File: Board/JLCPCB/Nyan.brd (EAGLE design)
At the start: 86 x 26 mm, 64 parts, among them Q1 8M, Q2 32768, U1 R-78C5.0-1.0, U3 A4988_STEP, U4 MAX6966, U5 ST3485, U6 74HCT541PW, U7 74HCT541PW, U8 STM32F10XCXT6, X1 WR-WTB2.0-2_THT-VER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

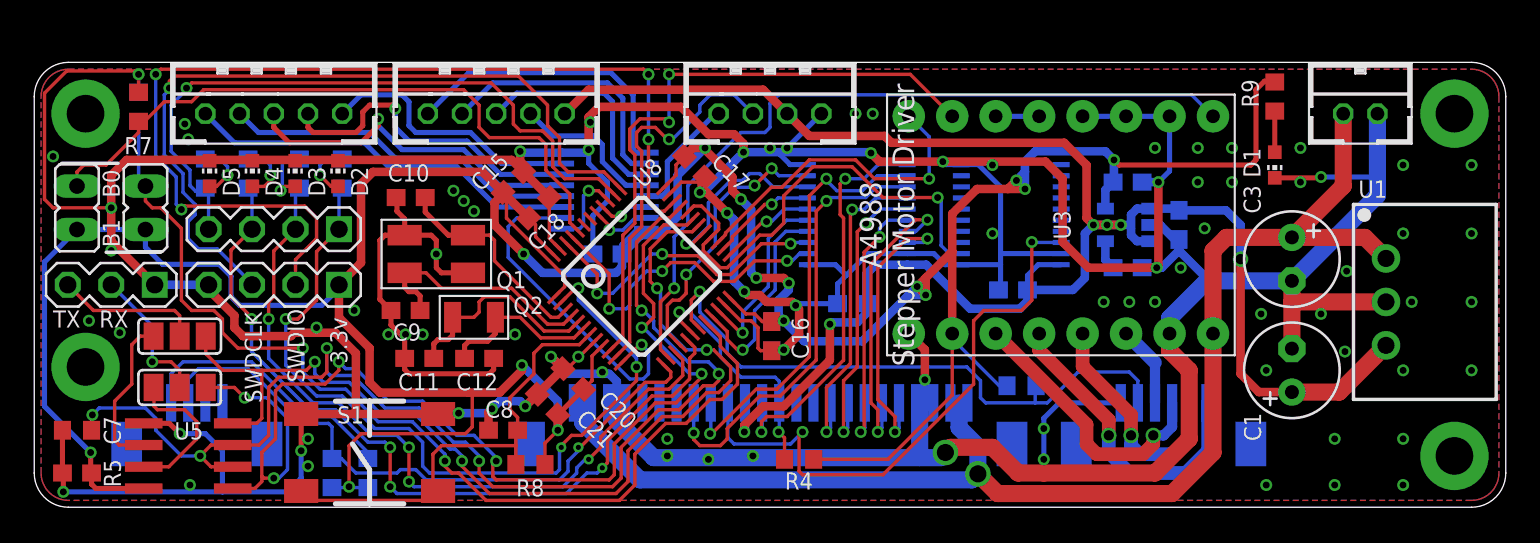
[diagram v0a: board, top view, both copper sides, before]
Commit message: [Board] Silkscreen done, DRC checked
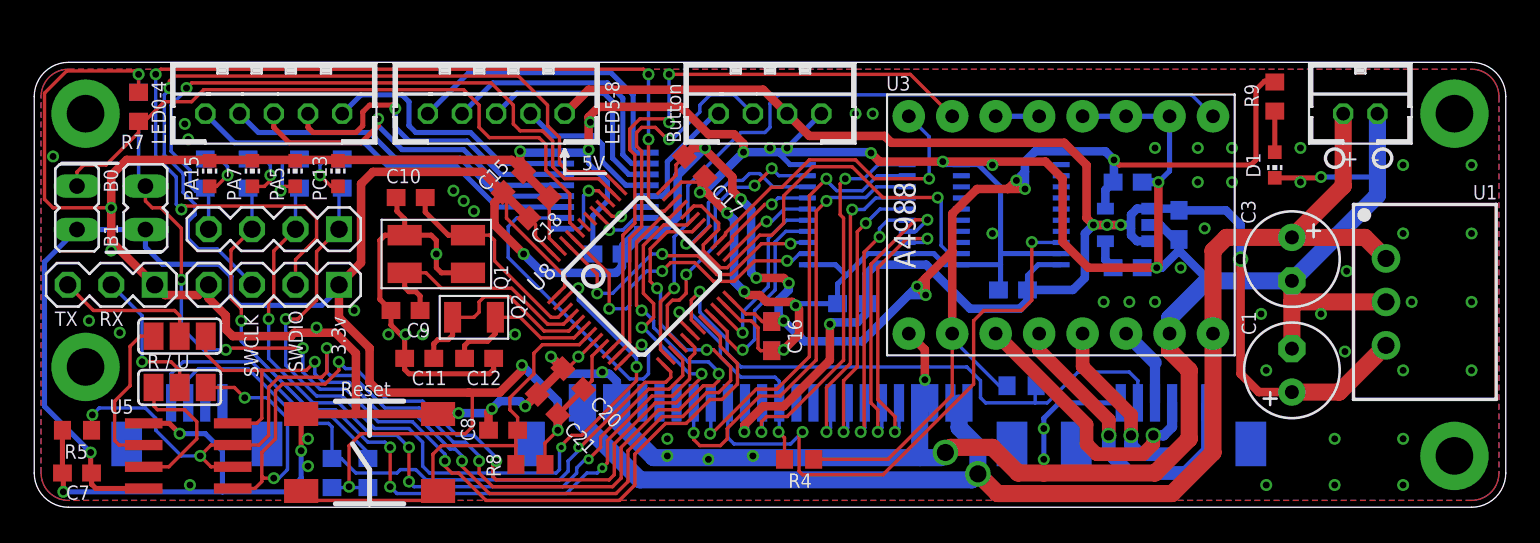
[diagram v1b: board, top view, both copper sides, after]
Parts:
- U3: device robotics:A4988_STEP -> IC:A4988_STEP
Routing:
- net GND: track 392.3 -> 393.4 mm
- net BOOT1: track 59.5 -> 60.1 mm, vias 2 -> 4
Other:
- board text added: "+ -"
- board text added: "5V"
- board text added: "Button"
- board text added: "LED0-4"
- board text added: "LED5-8"
- board text added: "PA15"
- board text added: "PA5"
- board text added: "PA7"
- board text added: "PC13"
- board text added: "R / U"
- board text added: "Reset"
- board text added: "SWCLK"
- board text removed: "SWDCLK"

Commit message: [Board] Fixed connection for crystals
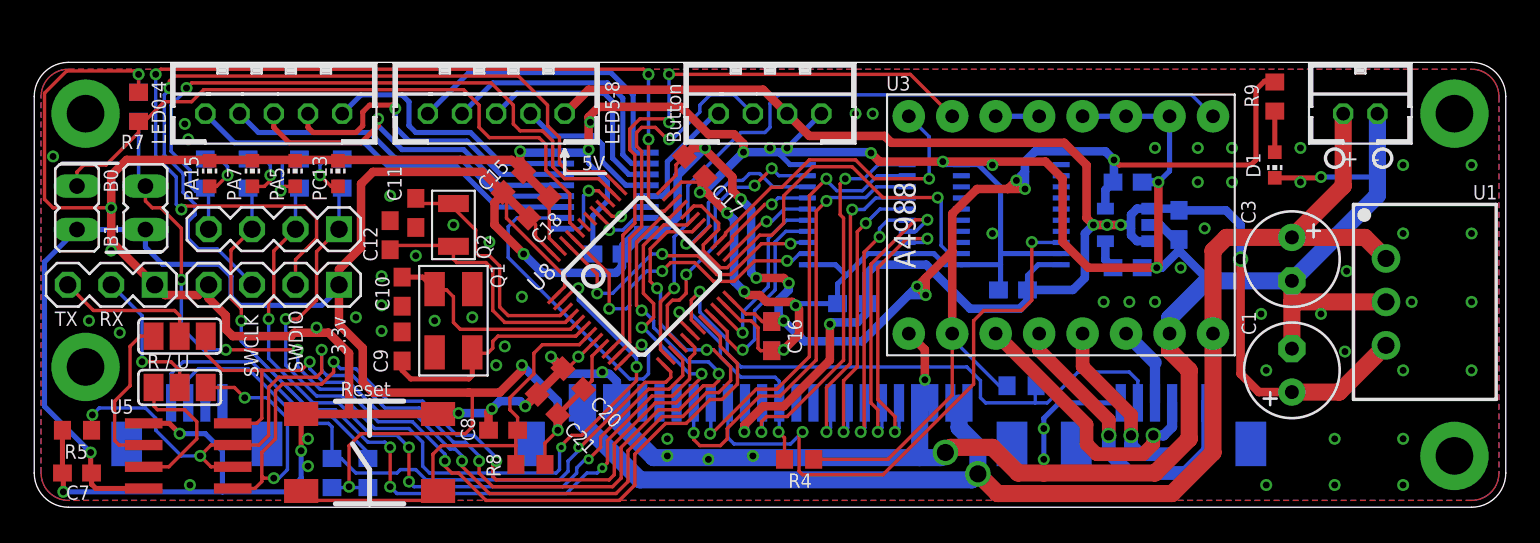
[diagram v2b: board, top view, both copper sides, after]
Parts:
- moved C12 8.88 mm to (20.8, 15.9), turned to 90 degrees
- moved C11 8.50 mm to (22.3, 17.2), turned to 270 degrees
- moved Q2 5.53 mm to (24.5, 16.5), turned to 90 degrees
- moved C10 5.52 mm to (21.5, 12.6), turned to 270 degrees
- moved Q1 4.03 mm to (24.5, 10.9), turned to 90 degrees
- moved C9 2.11 mm to (21.5, 9.40), turned to 90 degrees
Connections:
- net N$10: now also U8.3; no longer U8.5
- net N$11: now also U8.5; no longer U8.3
- net N$14: now also U8.6; no longer U8.4
- net N$9: now also U8.4; no longer U8.6
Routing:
- net GND: track 393.4 -> 369.3 mm, vias 88 -> 92
- net N$9: track 9.94 -> 14.6 mm
- net N$10: track 12.4 -> 14.1 mm

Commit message: [Board] Added debouncing circuitry for pushbutton
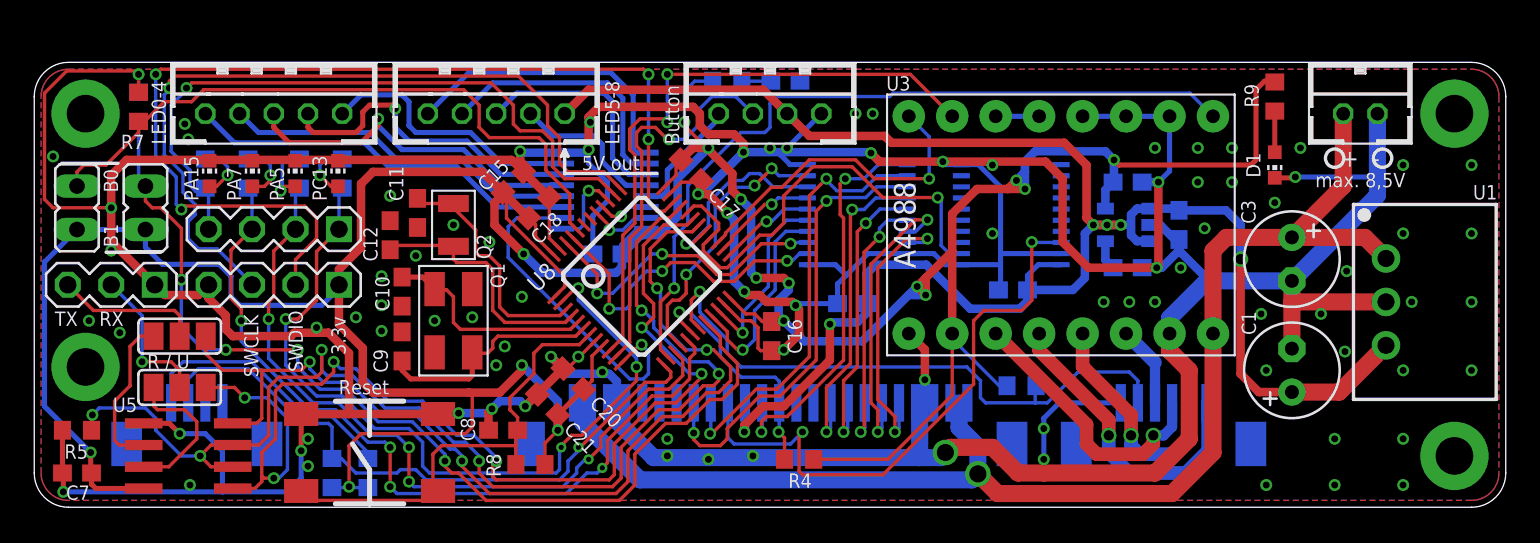
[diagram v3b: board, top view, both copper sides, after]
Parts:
- added C22: 100n, rcl:C0603
- added R14: 10k, rcl:R0603
- moved C17 0.28 mm to (38.4, 19.7)
- moved C11 0.10 mm to (22.4, 17.2)
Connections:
- net +3V3: now also R14.1
- net BUT_SIG: now also C22.1, R14.2
- net GND: now also C22.2, X8.2
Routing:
- net +3V3: track 226.5 -> 232.5 mm, vias 15 -> 16
- net BUT_SIG: track 22.9 -> 25.9 mm
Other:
- board text added: "5V out"
- board text added: "max. 8,5V"
- board text removed: "5V"

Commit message: [Board] Finished for manufacturing
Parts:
- moved SJ1 0.70 mm to (8.50, 9.30)
- moved C5 0.10 mm to (57.2, 12.8)
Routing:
- net RS485_A: track 9.31 -> 11.8 mm, vias 0 -> 2
- net TX: track 58.5 -> 57.8 mm
- net A/TX: track 8.49 -> 9.19 mm
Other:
- board text added: "0"
- board text added: "1"
- board text added: "2"
- board text added: "3"
- board text added: "4"
- board text added: "5"
- board text added: "5V"
- board text added: "6"
- board text added: "7"
- board text added: "8"
- board text added: "GND"
- board text added: "LED"
- board text added: "RS485"
- board text added: "SIG"
- board text added: "UART"
- board text removed: "5V out"
- board text removed: "R / U"
